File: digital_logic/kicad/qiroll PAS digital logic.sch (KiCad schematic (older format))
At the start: 18 parts, among them U1 14538, U2 4023, U3 4027, U4 14538

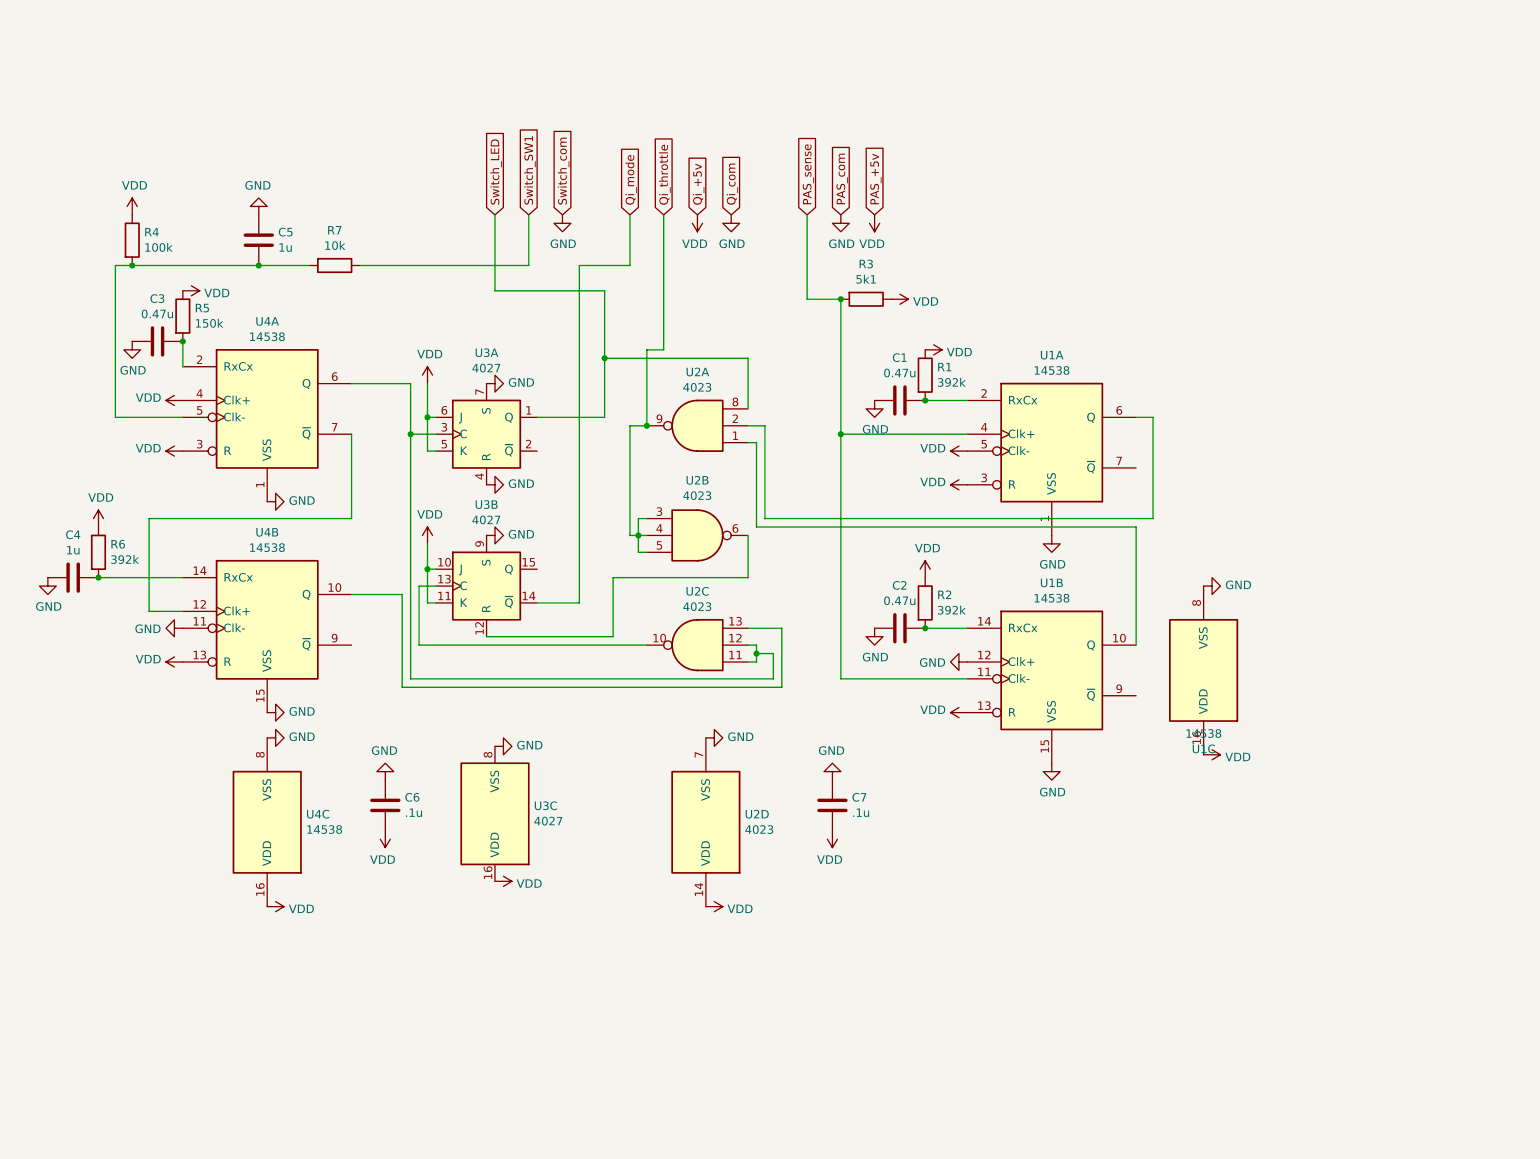
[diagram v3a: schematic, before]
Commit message: annotate schematic, voltage regulator, photos
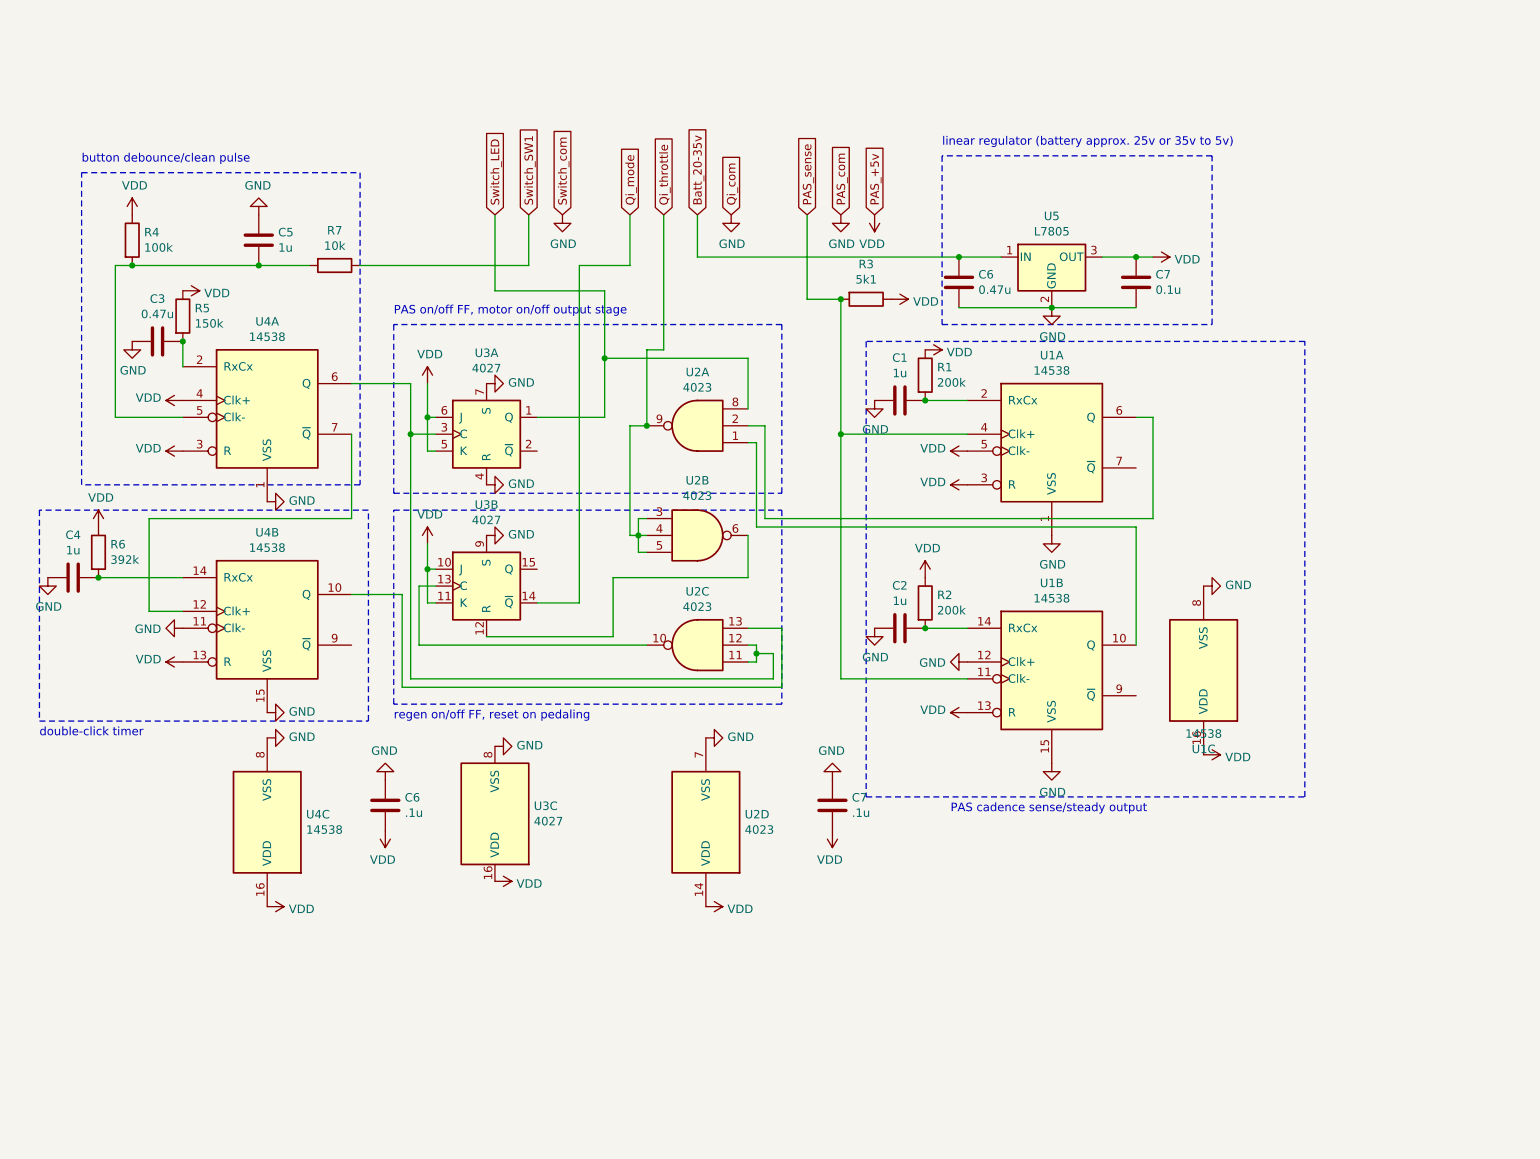
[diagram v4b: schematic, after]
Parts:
- added C6: 0.47u, symbol Device:C
- added C7: 0.1u, symbol Device:C
- added U5: L7805, symbol Regulator_Linear:L7805
- C1, C2: value 0.47u -> 1u
- R1, R2: value 392k -> 200k
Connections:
- net GND: now also C6.2, C7.2, U5.2 (GND)
- net VDD: now also C7.1, U5.3 (OUT)
- new net Batt_20-35v: C6.1, U5.1 (IN)
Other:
- note added: "PAS cadence sense/steady output"
- note added: "PAS on/off FF, motor on/off output stage"
- note added: "button debounce/clean pulse"
- note added: "double-click timer"
- note added: "linear regulator (battery approx. 25v or 35v to 5v)"
- note added: "regen on/off FF, reset on pedaling"
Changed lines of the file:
@@
 P 7650 2450
 F 0 "R1" H 7720 2496 50  0000 L CNN
-F 1 "392k" H 7720 2405 50  0000 L CNN
+F 1 "200k" H 7720 2405 50  0000 L CNN
 F 2 "" V 7580 2450 50  0001 C CNN
 F 3 "~" H 7650 2450 50  0001 C CNN
@@
 P 7650 3800
 F 0 "R2" H 7720 3846 50  0000 L CNN
-F 1 "392k" H 7720 3755 50  0000 L CNN
+F 1 "200k" H 7720 3755 50  0000 L CNN
 F 2 "" V 7580 3800 50  0001 C CNN
 F 3 "~" H 7650 3800 50  0001 C CNN
@@
 Qi_mode
 Text GLabel 6300 1500 1    50   Input ~ 0
-Qi_+5v
+Batt_20-35v
 Text GLabel 6500 1500 1    50   Input ~ 0
 Qi_com
@@
 	1    0    0    -1
 $EndComp
-$Comp
-L power:VDD #PWR?
-U 1 1 602BC0B1
-P 6300 1500
-F 0 "#PWR?" H 6300 1350 50  0001 C CNN
-F 1 "VDD" H 6315 1673 50  0000 C CNN
-F 2 "" H 6300 1500 50  0001 C CNN
-F 3 "" H 6300 1500 50  0001 C CNN
-	1    6300 1500
-	-1   0    0    1
-$EndComp
 Wire Wire Line
 	6000 2300 6100 2300
@@
 P 7500 3950
 F 0 "C2" V 7248 3950 50  0000 C CNN
-F 1 "0.47u" V 7339 3950 50  0000 C CNN
+F 1 "1u" V 7339 3950 50  0000 C CNN
 F 2 "" H 7538 3800 50  0001 C CNN
 F 3 "~" H 7500 3950 50  0001 C CNN
@@
 P 7500 2600
 F 0 "C1" V 7248 2600 50  0000 C CNN
-F 1 "0.47u" V 7339 2600 50  0000 C CNN
+F 1 "1u" V 7339 2600 50  0000 C CNN
 F 2 "" H 7538 2450 50  0001 C CNN
 F 3 "~" H 7500 2600 50  0001 C CNN
@@
 	-1   0    0    1
 $EndComp
+Wire Wire Line
+	6300 1500 6300 1750
+Wire Wire Line
+	6300 1750 7850 1750
+$Comp
+L power:VDD #PWR?
+U 1 1 6063EB88
+P 9000 1750
+F 0 "#PWR?" H 9000 1600 50  0001 C CNN
+F 1 "VDD" V 9015 1878 50  0000 L CNN
+F 2 "" H 9000 1750 50  0001 C CNN
+F 3 "" H 9000 1750 50  0001 C CNN
+	1    9000 1750
+	0    1    1    0
+$EndComp
+$Comp
+L Device:C C7
+U 1 1 606431FB
+P 8900 1900
+F 0 "C7" H 9015 1946 50  0000 L CNN
+F 1 "0.1u" H 9015 1855 50  0000 L CNN
+F 2 "" H 8938 1750 50  0001 C CNN
+F 3 "~" H 8900 1900 50  0001 C CNN
+	1    8900 1900
+	1    0    0    -1
+$EndComp
+Connection ~ 8900 1750
+Wire Wire Line
+	8900 1750 9000 1750
+$Comp
+L Device:C C6
+U 1 1 60646E8A
+P 7850 1900
+F 0 "C6" H 7965 1946 50  0000 L CNN
+F 1 "0.47u" H 7965 1855 50  0000 L CNN
+F 2 "" H 7888 1750 50  0001 C CNN
+F 3 "~" H 7850 1900 50  0001 C CNN
+	1    7850 1900
+	1    0    0    -1
+$EndComp
+Connection ~ 7850 1750
+Wire Notes Line
+	7300 2250 7300 4950
+Wire Notes Line
+	7300 4950 9900 4950
+Wire Notes Line
+	9900 4950 9900 2250
+Wire Notes Line
+	9900 2250 7300 2250
+Wire Notes Line
+	7750 1150 7750 2150
+Wire Notes Line
+	7750 2150 9350 2150
+Wire Notes Line
+	9350 2150 9350 1150
+Wire Notes Line
+	9350 1150 7750 1150
+Wire Notes Line
+	4500 2150 4500 3150
+Wire Notes Line
+	4500 3150 6800 3150
+Wire Notes Line
+	6800 3150 6800 2150
+Wire Notes Line
+	6800 2150 4500 2150
+Wire Notes Line
+	4500 3250 6800 3250
+Wire Notes Line
+	6800 3250 6800 4400
+Wire Notes Line
+	6800 4400 4500 4400
+Wire Notes Line
+	4500 4400 4500 3250
+Wire Notes Line
+	4300 1250 4300 3100
+Wire Notes Line
+	4300 3100 2650 3100
+Wire Notes Line
+	2650 3100 2650 1250
+Wire Notes Line
+	2650 1250 4300 1250
+Wire Notes Line
+	2400 3250 2400 4500
+Wire Notes Line
+	2400 4500 4350 4500
+Wire Notes Line
+	4350 4500 4350 3250
+Wire Notes Line
+	4350 3250 2400 3250
+Text Notes 7800 5050 0    50   ~ 0
+PAS cadence sense/steady output
+Text Notes 7750 1100 0    50   ~ 0
+linear regulator (battery approx. 25v or 35v to 5v)
+Text Notes 4500 2100 0    50   ~ 0
+PAS on/off FF, motor on/off output stage
+Text Notes 4500 4500 0    50   ~ 0
+regen on/off FF, reset on pedaling
+Text Notes 2650 1200 0    50   ~ 0
+button debounce/clean pulse
+Text Notes 2400 4600 0    50   ~ 0
+double-click timer
+$Comp
+L Regulator_Linear:L7805 U5
+U 1 1 6066B66B
+P 8400 1750
+F 0 "U5" H 8400 1992 50  0000 C CNN
+F 1 "L7805" H 8400 1901 50  0000 C CNN
+F 2 "" H 8425 1600 50  0001 L CIN
+F 3 "http://www.st.com/content/ccc/resource/technical/document/datasheet/41/4f/b3/b0/12/d4/47/88/CD00000444.pdf/files/CD00000444.pdf/jcr:content/translations/en.CD00000444.pdf" H 8400 1700 50  0001 C CNN
+	1    8400 1750
+	1    0    0    -1
+$EndComp
+Wire Wire Line
+	7850 1750 8100 1750
+Wire Wire Line
+	8700 1750 8900 1750
+$Comp
+L power:GND #PWR?
+U 1 1 60683075
+P 8400 2050
+F 0 "#PWR?" H 8400 1800 50  0001 C CNN
+F 1 "GND" H 8405 1877 50  0000 C CNN
+F 2 "" H 8400 2050 50  0001 C CNN
+F 3 "" H 8400 2050 50  0001 C CNN
+	1    8400 2050
+	1    0    0    -1
+$EndComp
+Wire Wire Line
+	7850 2050 8400 2050
+Connection ~ 8400 2050
+Wire Wire Line
+	8400 2050 8900 2050
 $EndSCHEMATC

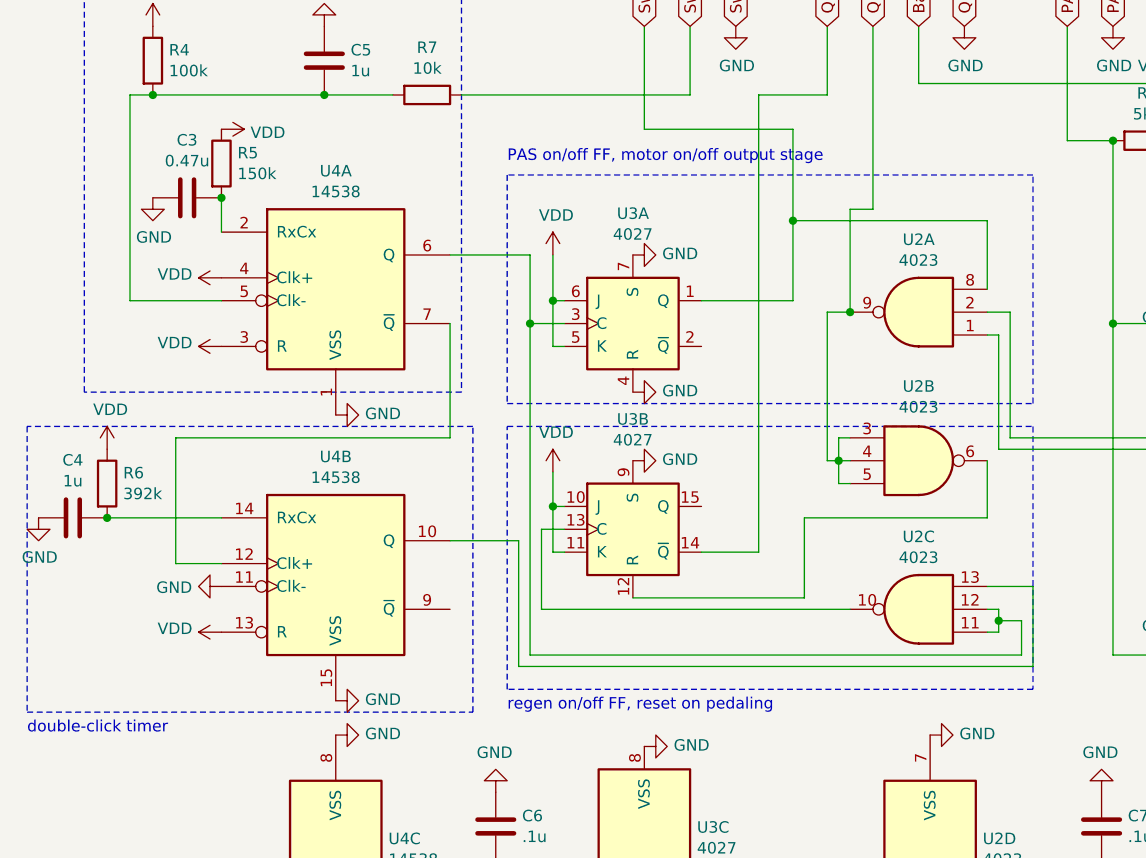
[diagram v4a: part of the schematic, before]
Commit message: fix schematic errors, swap 4023 units for ease of assembly
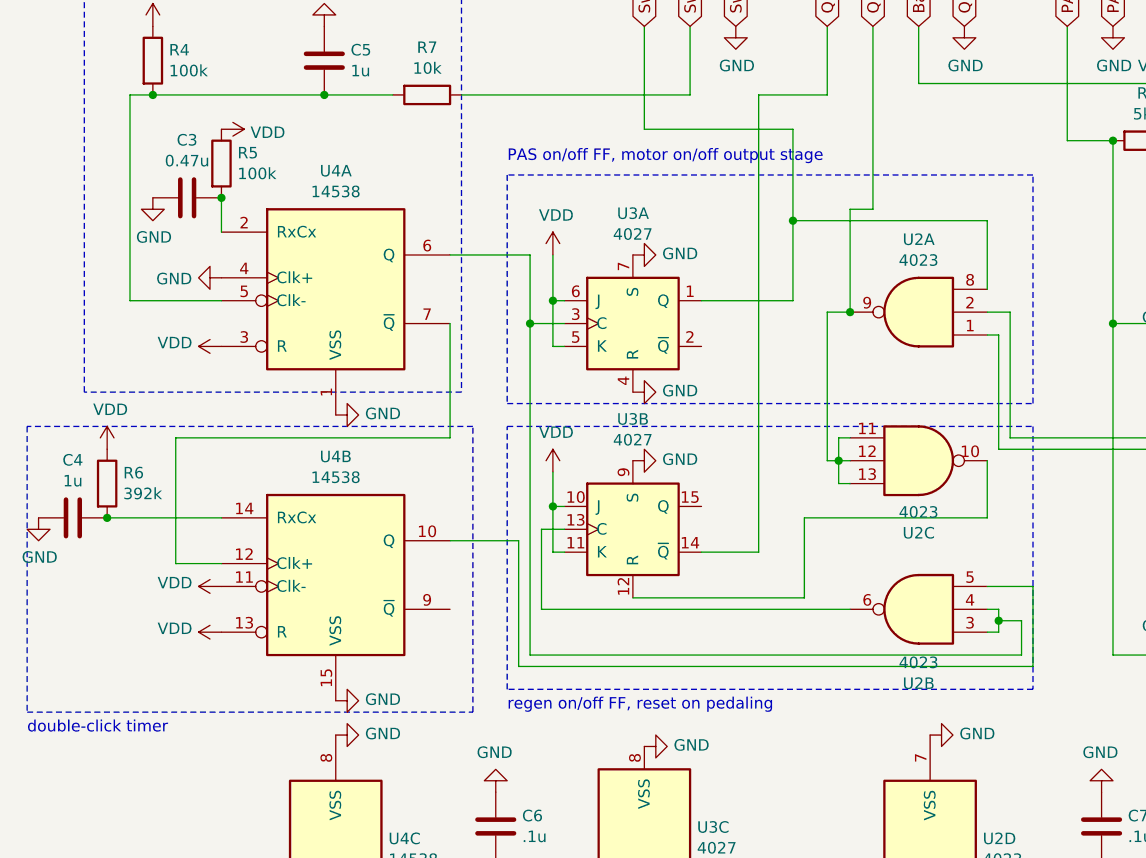
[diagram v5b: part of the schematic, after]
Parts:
- R5: value 150k -> 100k
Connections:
- net GND: now also U4.4 (Clk+); no longer U4.11 (Clk-)
- net Qi_throttle: now also U2.11, U2.12, U2.13; no longer U2.3, U2.4, U2.5
- net VDD: now also U4.11 (Clk-); no longer U4.4 (Clk+)
- net at U3.3 (C), U4.6 (Q): now also U2.3, U2.4; no longer U2.11, U2.12
- net at U3.12 (R): now also U2.10; no longer U2.6
- net at U3.13 (C): now also U2.6; no longer U2.10
- net at U4.10 (Q): now also U2.5; no longer U2.13
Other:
- moved on the sheet: U2B, U2C
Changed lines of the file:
@@
 L 4xxx:4023 U2
 U 2 1 6032F0EA
+P 6300 4050
+F 0 "U2" H 6300 4375 50  0000 C CNN
+F 1 "4023" H 6300 4284 50  0000 C CNN
+F 2 "" H 6300 4050 50  0001 C CNN
+F 3 "http://www.intersil.com/content/dam/Intersil/documents/cd40/cd4011bms-12bms-23bms.pdf" H 6300 4050 50  0001 C CNN
+	2    6300 4050
+	-1   0    0    1
+$EndComp
+$Comp
+L 4xxx:4023 U2
+U 3 1 6033216D
 P 6300 3400
-F 0 "U2" H 6300 3725 50  0000 C CNN
-F 1 "4023" H 6300 3634 50  0000 C CNN
+F 0 "U2" H 6300 3083 50  0000 C CNN
+F 1 "4023" H 6300 3174 50  0000 C CNN
 F 2 "" H 6300 3400 50  0001 C CNN
 F 3 "http://www.intersil.com/content/dam/Intersil/documents/cd40/cd4011bms-12bms-23bms.pdf" H 6300 3400 50  0001 C CNN
-	2    6300 3400
-	1    0    0    -1
-$EndComp
-$Comp
-L 4xxx:4023 U2
-U 3 1 6033216D
-P 6300 4050
-F 0 "U2" H 6300 3733 50  0000 C CNN
-F 1 "4023" H 6300 3824 50  0000 C CNN
-F 2 "" H 6300 4050 50  0001 C CNN
-F 3 "http://www.intersil.com/content/dam/Intersil/documents/cd40/cd4011bms-12bms-23bms.pdf" H 6300 4050 50  0001 C CNN
-	3    6300 4050
-	-1   0    0    1
+	3    6300 3400
+	1    0    0    -1
 $EndComp
 $Comp
@@
 Wire Wire Line
 	4250 3300 3050 3300
-$Comp
-L power:GND #PWR?
-U 1 1 60371511
-P 3250 3950
-F 0 "#PWR?" H 3250 3700 50  0001 C CNN
-F 1 "GND" V 3255 3822 50  0000 R CNN
-F 2 "" H 3250 3950 50  0001 C CNN
-F 3 "" H 3250 3950 50  0001 C CNN
-	1    3250 3950
-	0    1    1    0
-$EndComp
-$Comp
-L power:VDD #PWR?
-U 1 1 603728C0
-P 3250 2600
-F 0 "#PWR?" H 3250 2450 50  0001 C CNN
-F 1 "VDD" V 3265 2727 50  0000 L CNN
-F 2 "" H 3250 2600 50  0001 C CNN
-F 3 "" H 3250 2600 50  0001 C CNN
-	1    3250 2600
-	0    -1   -1   0
-$EndComp
 Wire Wire Line
 	2850 1800 2850 2700
@@
 P 3250 2100
 F 0 "R5" H 3320 2146 50  0000 L CNN
-F 1 "150k" H 3320 2055 50  0000 L CNN
+F 1 "100k" H 3320 2055 50  0000 L CNN
 F 2 "" V 3180 2100 50  0001 C CNN
 F 3 "~" H 3250 2100 50  0001 C CNN
@@
 Wire Wire Line
 	8400 2050 8900 2050
+$Comp
+L power:VDD #PWR?
+U 1 1 606C0841
+P 3250 3950
+F 0 "#PWR?" H 3250 3800 50  0001 C CNN
+F 1 "VDD" V 3265 4077 50  0000 L CNN
+F 2 "" H 3250 3950 50  0001 C CNN
+F 3 "" H 3250 3950 50  0001 C CNN
+	1    3250 3950
+	0    -1   -1   0
+$EndComp
+$Comp
+L power:GND #PWR?
+U 1 1 606CBEF8
+P 3250 2600
+F 0 "#PWR?" H 3250 2350 50  0001 C CNN
+F 1 "GND" V 3255 2472 50  0000 R CNN
+F 2 "" H 3250 2600 50  0001 C CNN
+F 3 "" H 3250 2600 50  0001 C CNN
+	1    3250 2600
+	0    1    1    0
+$EndComp
 $EndSCHEMATC
